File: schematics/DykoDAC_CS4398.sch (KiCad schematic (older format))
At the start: 22 parts, among them U8 CS4398, X1 22.5792Mhz, X2 24.576Mhz

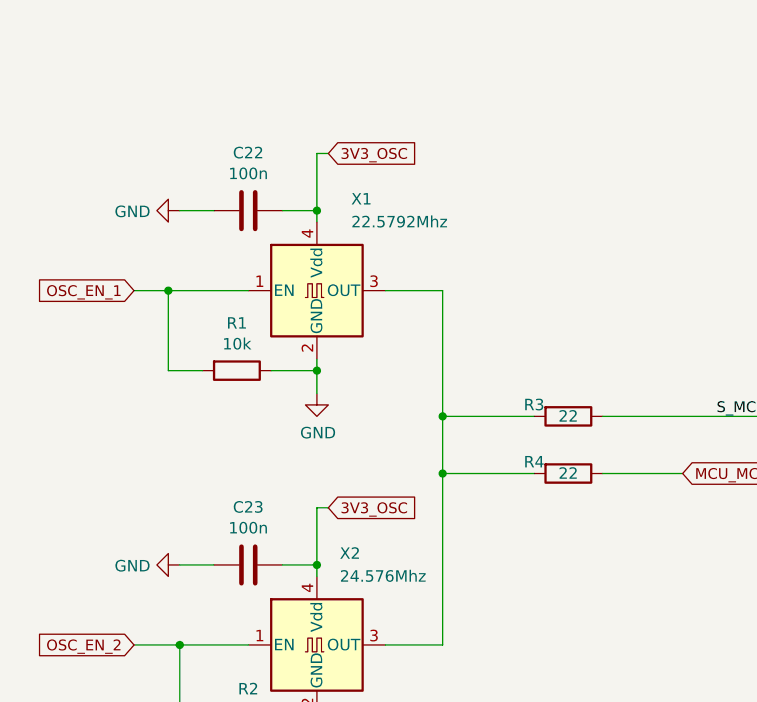
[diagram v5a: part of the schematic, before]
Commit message: opamp filter pcb
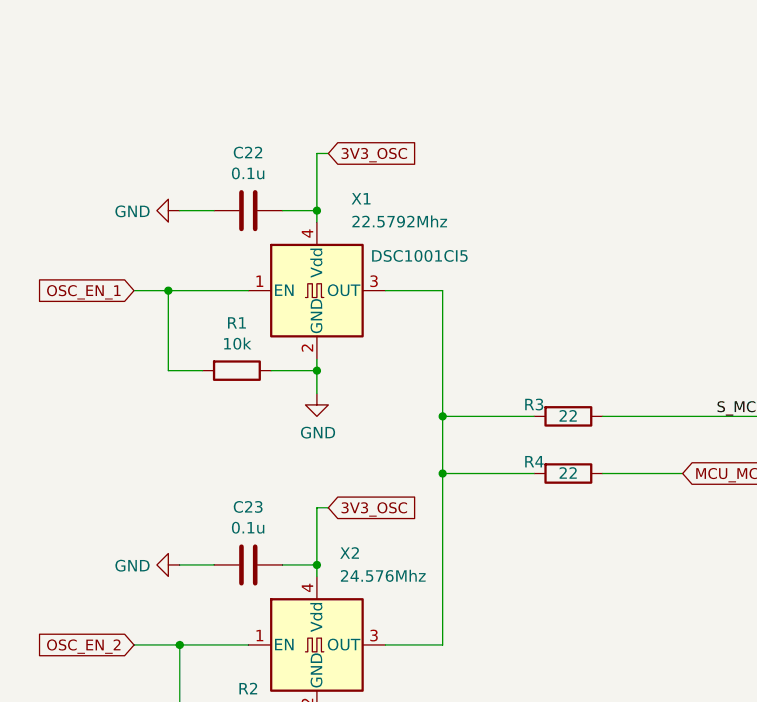
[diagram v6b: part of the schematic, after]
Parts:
- C22, C23: value 100n -> 0.1u
- C26, C29, C33: footprint Capacitors_SMD:CP_Elec_4x5.7 -> Capacitors_Tantalum_SMD:CP_Tantalum_Case-A_EIA-3216-18_Reflow
- C32: footprint Capacitors_SMD:CP_Elec_6.3x5.8 -> Capacitors_Tantalum_SMD:CP_Tantalum_Case-D_EIA-7343-31_Reflow; Part (none) -> TAJD107K016SNJ
- C34: footprint Capacitors_SMD:CP_Elec_4x5.7 -> Capacitors_Tantalum_SMD:CP_Tantalum_Case-B_EIA-3528-21_Reflow
- X1: footprint Oscillators:Oscillator_SMD_TXC_7C-4pin_5.0x3.2mm_HandSoldering -> Oscillators:Oscillator_SMD_Abracon_ASE-4pin_3.2x2.5mm; Part (none) -> DSC1001CI5
- X2: footprint Oscillators:Oscillator_SMD_TXC_7C-4pin_5.0x3.2mm_HandSoldering -> Oscillators:Oscillator_SMD_Abracon_ASE-4pin_3.2x2.5mm
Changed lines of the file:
@@
 F 0 "C26" H 7282 1654 50  0000 R CNN
 F 1 "10u" H 7282 1745 50  0000 R CNN
-F 2 "Capacitors_SMD:CP_Elec_4x5.7" H 7438 1550 50  0001 C CNN
+F 2 "Capacitors_Tantalum_SMD:CP_Tantalum_Case-A_EIA-3216-18_Reflow" H 7438 1550 50  0001 C CNN
 F 3 "~" H 7400 1700 50  0001 C CNN
 	1    7400 1700
@@
 F 0 "C29" H 8532 1654 50  0000 R CNN
 F 1 "10u" H 8532 1745 50  0000 R CNN
-F 2 "Capacitors_SMD:CP_Elec_4x5.7" H 8688 1550 50  0001 C CNN
+F 2 "Capacitors_Tantalum_SMD:CP_Tantalum_Case-A_EIA-3216-18_Reflow" H 8688 1550 50  0001 C CNN
 F 3 "~" H 8650 1700 50  0001 C CNN
 	1    8650 1700
@@
 F 0 "C32" H 9800 3900 50  0000 L CNN
 F 1 "100u" H 9800 3700 50  0000 L CNN
-F 2 "Capacitors_SMD:CP_Elec_6.3x5.8" H 9788 3650 50  0001 C CNN
+F 2 "Capacitors_Tantalum_SMD:CP_Tantalum_Case-D_EIA-7343-31_Reflow" H 9788 3650 50  0001 C CNN
 F 3 "~" H 9750 3800 50  0001 C CNN
+F 4 "TAJD107K016SNJ" H 9750 3800 50  0001 C CNN "Part"
 	1    9750 3800
 	1    0    0    -1
@@
 F 0 "C33" H 9632 4204 50  0000 R CNN
 F 1 "33u" H 9632 4295 50  0000 R CNN
-F 2 "Capacitors_SMD:CP_Elec_4x5.7" H 9788 4100 50  0001 C CNN
+F 2 "Capacitors_Tantalum_SMD:CP_Tantalum_Case-A_EIA-3216-18_Reflow" H 9788 4100 50  0001 C CNN
 F 3 "~" H 9750 4250 50  0001 C CNN
 	1    9750 4250
@@
 Wire Wire Line
 	9450 3600 9750 3600
-$Comp
-L Device:CP C34
-U 1 1 5C8FCF01
-P 10150 3800
-F 0 "C34" H 10268 3846 50  0000 L CNN
-F 1 "3.3u" H 10268 3755 50  0000 L CNN
-F 2 "Capacitors_SMD:CP_Elec_4x5.7" H 10188 3650 50  0001 C CNN
-F 3 "~" H 10150 3800 50  0001 C CNN
-	1    10150 3800
-	1    0    0    -1
-$EndComp
 Wire Wire Line
 	8950 3650 9100 3650
@@
 F 0 "X1" H 2800 5100 50  0000 L CNN
 F 1 "22.5792Mhz" H 2800 5000 50  0000 L CNN
-F 2 "Oscillators:Oscillator_SMD_TXC_7C-4pin_5.0x3.2mm_HandSoldering" H 3350 4350 50  0001 C CNN
+F 2 "Oscillators:Oscillator_SMD_Abracon_ASE-4pin_3.2x2.5mm" H 3350 4350 50  0001 C CNN
 F 3 "http://www.txccorp.com/download/products/osc/7C_o.pdf" H 2550 4700 50  0001 C CNN
+F 4 "DSC1001CI5" H 3100 4850 50  0000 C CNN "Part"
 	1    2650 4700
 	1    0    0    -1
@@
 F 0 "X2" H 2750 6650 50  0000 L CNN
 F 1 "24.576Mhz" H 2750 6550 50  0000 L CNN
-F 2 "Oscillators:Oscillator_SMD_TXC_7C-4pin_5.0x3.2mm_HandSoldering" H 3350 5900 50  0001 C CNN
+F 2 "Oscillators:Oscillator_SMD_Abracon_ASE-4pin_3.2x2.5mm" H 3350 5900 50  0001 C CNN
 F 3 "http://www.txccorp.com/download/products/osc/7C_o.pdf" H 2550 6250 50  0001 C CNN
 	1    2650 6250
@@
 AR Path="/5C8F8588/5D1FEDA4" Ref="C23"  Part="1"
 F 0 "C23" V 2098 5900 50  0000 C CNN
-F 1 "100n" V 2189 5900 50  0000 C CNN
+F 1 "0.1u" V 2189 5900 50  0000 C CNN
 F 2 "Capacitors_SMD:C_0603" H 2388 5750 50  0001 C CNN
 F 3 "~" H 2350 5900 50  0001 C CNN
@@
 AR Path="/5C8F8588/5D1FEDB4" Ref="C22"  Part="1"
 F 0 "C22" V 2098 4350 50  0000 C CNN
-F 1 "100n" V 2189 4350 50  0000 C CNN
+F 1 "0.1u" V 2189 4350 50  0000 C CNN
 F 2 "Capacitors_SMD:C_0603" H 2388 4200 50  0001 C CNN
 F 3 "~" H 2350 4350 50  0001 C CNN
@@
 NoConn ~ 8950 2450
 NoConn ~ 8950 3450
+$Comp
+L Device:CP C34
+U 1 1 5E63FCBA
+P 10150 3800
+F 0 "C34" H 10268 3846 50  0000 L CNN
+F 1 "3.3u" H 10268 3755 50  0000 L CNN
+F 2 "Capacitors_Tantalum_SMD:CP_Tantalum_Case-B_EIA-3528-21_Reflow" H 10188 3650 50  0001 C CNN
+F 3 "~" H 10150 3800 50  0001 C CNN
+	1    10150 3800
+	1    0    0    -1
+$EndComp
 $EndSCHEMATC

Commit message: pcb
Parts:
- removed C34: 3.3u, Capacitors_Tantalum_SMD:CP_Tantalum_Case-B_EIA-3528-21_Reflow, symbol Device:CP
- removed R5, R6: 10k, Resistors_SMD:R_0603, symbol Device:R
- added C34: 3.3u, Capacitors_SMD:C_0805, symbol Device:C
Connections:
- net GND: now also C34.2
- net at U8.26 (VQ): now also C34.1
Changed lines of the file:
@@
 $EndDescr
-$Comp
-L DykoDAC-rescue:CS4398-cirrus-2 U?
-U 1 1 5C8F866A
-P 8050 3350
-AR Path="/5C8F866A" Ref="U?"  Part="1"
-AR Path="/5C8F8588/5C8F866A" Ref="U8"  Part="1"
-F 0 "U8" H 8050 3400 50  0000 C CNN
-F 1 "CS4398" H 8050 3300 50  0000 C CNN
-F 2 "Housings_SSOP:TSSOP-28_4.4x9.7mm_Pitch0.65mm" H 8050 3500 50  0001 C CNN
-F 3 "" H 8050 3350 50  0001 C CNN
-	1    8050 3350
-	1    0    0    -1
-$EndComp
 $Comp
 L Device:C C27
@@
 Connection ~ 9450 4500
 Wire Wire Line
-	9450 4500 9150 4500
-Wire Wire Line
 	9750 3650 9750 3600
 Wire Wire Line
@@
 Text GLabel 6750 4250 0    50   Input ~ 0
 DAC_RST
-Wire Wire Line
-	7150 4250 6900 4250
-$Comp
-L Device:R R6
-U 1 1 5C8EA06B
-P 6900 4600
-F 0 "R6" H 6830 4554 50  0000 R CNN
-F 1 "10k" H 6830 4645 50  0000 R CNN
-F 2 "Resistors_SMD:R_0603" V 6830 4600 50  0001 C CNN
-F 3 "~" H 6900 4600 50  0001 C CNN
-	1    6900 4600
-	-1   0    0    1
-$EndComp
-$Comp
-L power:+3V3 #PWR019
-U 1 1 5C8EA11A
-P 6900 4950
-F 0 "#PWR019" H 6900 4800 50  0001 C CNN
-F 1 "+3V3" H 6915 5123 50  0000 C CNN
-F 2 "" H 6900 4950 50  0001 C CNN
-F 3 "" H 6900 4950 50  0001 C CNN
-	1    6900 4950
-	-1   0    0    1
-$EndComp
-Wire Wire Line
-	6900 4950 6900 4750
-Wire Wire Line
-	6900 4450 6900 4250
-Connection ~ 6900 4250
-Wire Wire Line
-	6900 4250 6750 4250
 Text GLabel 6450 3750 0    50   Input ~ 0
 DAC_CS
@@
 	5800 3650 5800 3550
 Connection ~ 5800 3550
-Wire Wire Line
-	5800 3550 6450 3550
-Wire Wire Line
-	6450 3750 6900 3750
-$Comp
-L Device:R R5
-U 1 1 5C8F4EB9
-P 6700 3650
-F 0 "R5" V 6650 3800 50  0000 C CNN
-F 1 "10k" V 6700 3650 50  0000 C CNN
-F 2 "Resistors_SMD:R_0603" V 6630 3650 50  0001 C CNN
-F 3 "~" H 6700 3650 50  0001 C CNN
-	1    6700 3650
-	0    -1   -1   0
-$EndComp
-Wire Wire Line
-	6850 3650 6900 3650
-Wire Wire Line
-	6900 3650 6900 3750
-Connection ~ 6900 3750
-Wire Wire Line
-	6900 3750 7150 3750
-Wire Wire Line
-	6550 3650 6450 3650
-Wire Wire Line
-	6450 3650 6450 3550
-Connection ~ 6450 3550
-Wire Wire Line
-	6450 3550 7150 3550
 Text GLabel 6550 4050 0    50   Input ~ 0
 MCU_MOSI
@@
 NoConn ~ 8950 3450
 $Comp
-L Device:CP C34
-U 1 1 5E63FCBA
+L Device:C C34
+U 1 1 5E999F0B
 P 10150 3800
-F 0 "C34" H 10268 3846 50  0000 L CNN
-F 1 "3.3u" H 10268 3755 50  0000 L CNN
-F 2 "Capacitors_Tantalum_SMD:CP_Tantalum_Case-B_EIA-3528-21_Reflow" H 10188 3650 50  0001 C CNN
+F 0 "C34" H 10265 3846 50  0000 L CNN
+F 1 "3.3u" H 10265 3755 50  0000 L CNN
+F 2 "Capacitors_SMD:C_0805" H 10188 3650 50  0001 C CNN
 F 3 "~" H 10150 3800 50  0001 C CNN
 	1    10150 3800
 	1    0    0    -1
 $EndComp
+Wire Wire Line
+	9450 4500 9150 4500
+$Comp
+L DykoDAC-rescue:CS4398-cirrus-2 U?
+U 1 1 5C8F866A
+P 8050 3350
+AR Path="/5C8F866A" Ref="U?"  Part="1"
+AR Path="/5C8F8588/5C8F866A" Ref="U8"  Part="1"
+F 0 "U8" H 8050 3400 50  0000 C CNN
+F 1 "CS4398" H 8050 3300 50  0000 C CNN
+F 2 "Housings_SSOP:TSSOP-28_4.4x9.7mm_Pitch0.65mm" H 8050 3500 50  0001 C CNN
+F 3 "" H 8050 3350 50  0001 C CNN
+	1    8050 3350
+	1    0    0    -1
+$EndComp
+Wire Wire Line
+	6750 4250 7150 4250
+Wire Wire Line
+	6450 3750 7150 3750
+Wire Wire Line
+	5800 3550 7150 3550
 $EndSCHEMATC

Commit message: pcb
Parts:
- X1: footprint Oscillators:Oscillator_SMD_Abracon_ASE-4pin_3.2x2.5mm -> Oscillators:Oscillator_SMD_SeikoEpson_SG210-4pin_2.5x2.0mm_HandSoldering; Part DSC1001CI5 -> NDK NZ2520SD
- X2: footprint Oscillators:Oscillator_SMD_Abracon_ASE-4pin_3.2x2.5mm -> Oscillators:Oscillator_SMD_SeikoEpson_SG210-4pin_2.5x2.0mm_HandSoldering
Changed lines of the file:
@@
 F 0 "X1" H 2800 5100 50  0000 L CNN
 F 1 "22.5792Mhz" H 2800 5000 50  0000 L CNN
-F 2 "Oscillators:Oscillator_SMD_Abracon_ASE-4pin_3.2x2.5mm" H 3350 4350 50  0001 C CNN
+F 2 "Oscillators:Oscillator_SMD_SeikoEpson_SG210-4pin_2.5x2.0mm_HandSoldering" H 3350 4350 50  0001 C CNN
 F 3 "http://www.txccorp.com/download/products/osc/7C_o.pdf" H 2550 4700 50  0001 C CNN
-F 4 "DSC1001CI5" H 3100 4850 50  0000 C CNN "Part"
+F 4 "NDK NZ2520SD" H 3200 4850 50  0000 C CNN "Part"
 	1    2650 4700
 	1    0    0    -1
@@
 F 0 "X2" H 2750 6650 50  0000 L CNN
 F 1 "24.576Mhz" H 2750 6550 50  0000 L CNN
-F 2 "Oscillators:Oscillator_SMD_Abracon_ASE-4pin_3.2x2.5mm" H 3350 5900 50  0001 C CNN
+F 2 "Oscillators:Oscillator_SMD_SeikoEpson_SG210-4pin_2.5x2.0mm_HandSoldering" H 3350 5900 50  0001 C CNN
 F 3 "http://www.txccorp.com/download/products/osc/7C_o.pdf" H 2550 6250 50  0001 C CNN
 	1    2650 6250
